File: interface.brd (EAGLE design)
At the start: 100 x 80 mm, 37 parts, among them U1 ATMEGA328P_PDIP

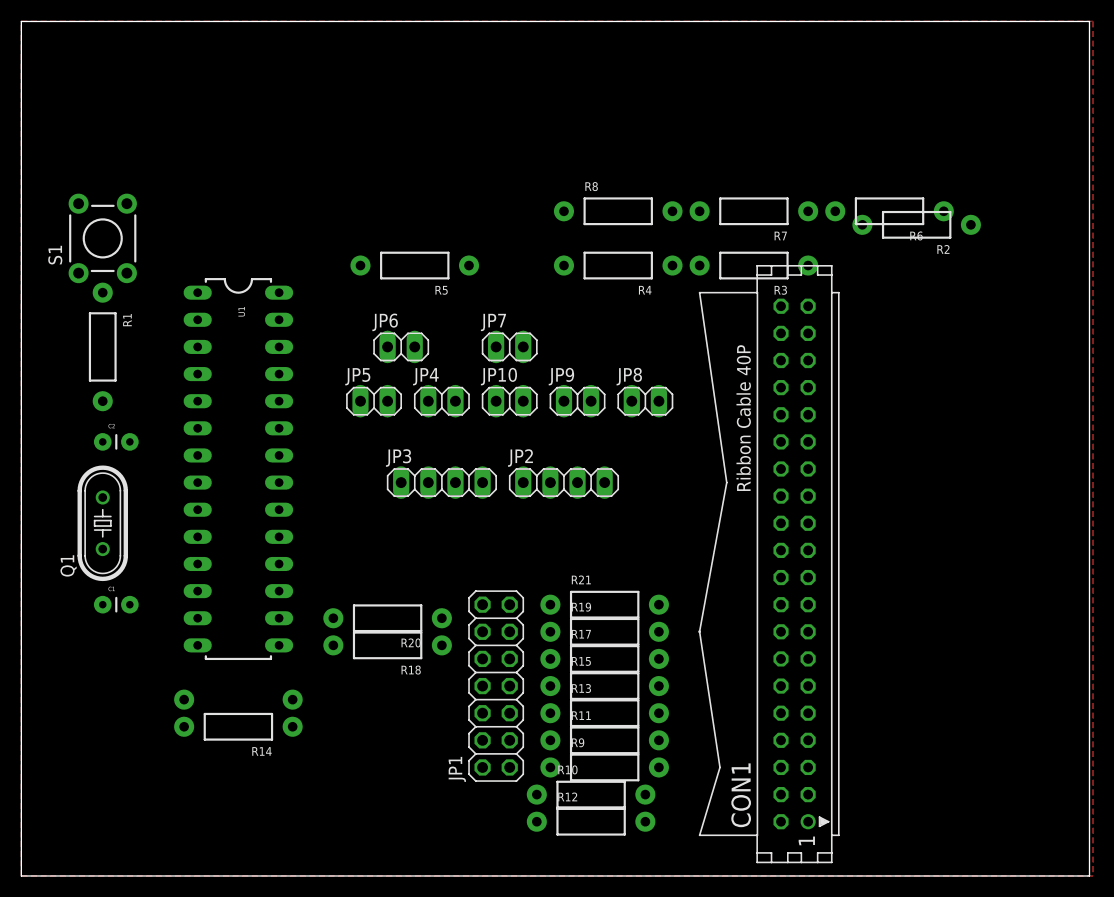
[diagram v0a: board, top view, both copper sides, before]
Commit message: Reorg the schematic. First pass at autorouter
Need to check if LED resistors will affect XBox circuitry
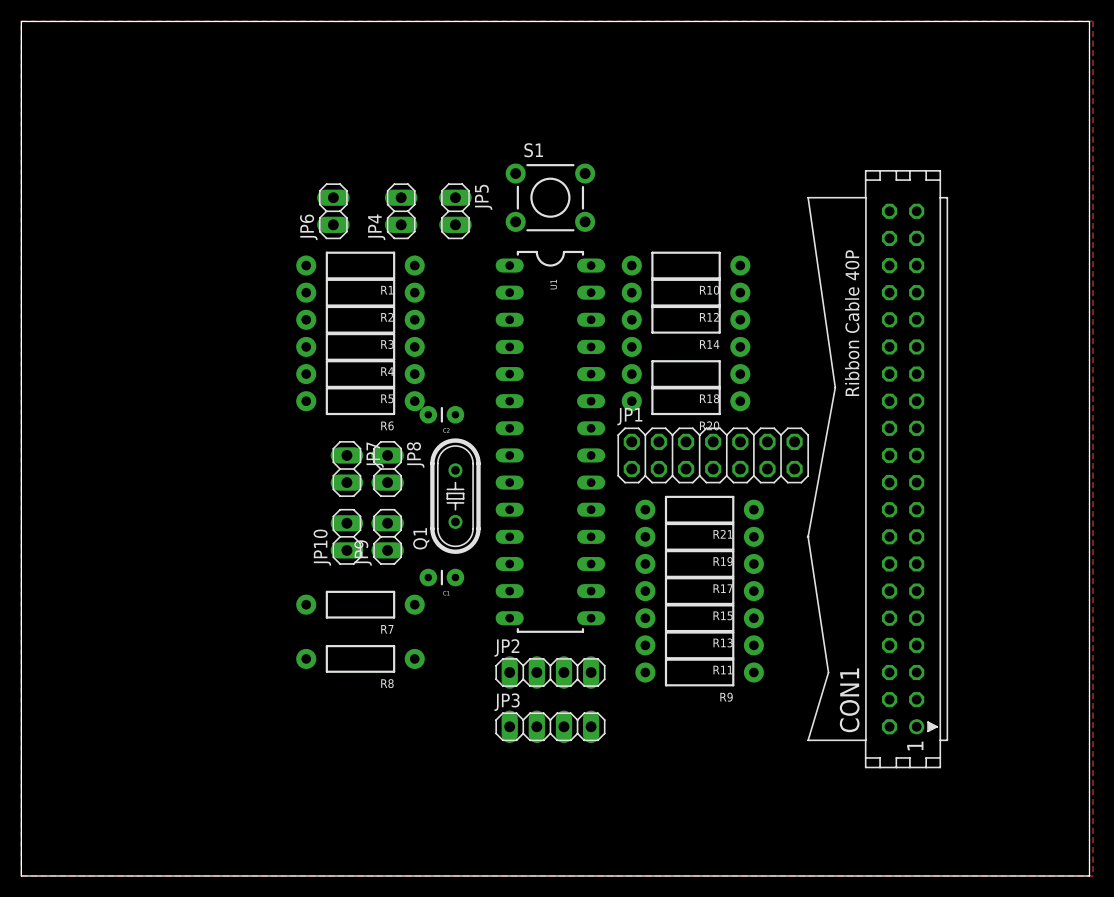
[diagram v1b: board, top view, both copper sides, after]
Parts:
- moved R14 56.6 mm to (62.2, 52.1)
- moved R16 53.4 mm to (62.2, 49.5)
- moved R6 52.6 mm to (31.8, 44.5)
- moved R2 52.5 mm to (31.8, 54.6)
- moved R7 52.1 mm to (31.8, 25.4)
- moved R10 50.3 mm to (62.2, 57.1), turned to 180 degrees
- moved R12 50.3 mm to (62.2, 54.6), turned to 180 degrees
- moved R8 48.4 mm to (31.8, 20.3), turned to 180 degrees
- moved S1 42.1 mm to (49.5, 63.5), turned to 0 degrees
- moved R18 37.8 mm to (62.2, 47.0)
- moved R3 37.2 mm to (31.8, 52.1)
- moved R20 34.5 mm to (62.2, 44.5)
- moved C1 33.1 mm to (40.6, 27.9), turned to 180 degrees
- moved C2 33.1 mm to (40.6, 43.2), turned to 180 degrees
- moved Q1 33.1 mm to (40.6, 35.6)
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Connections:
- net BTN1: now also U1.2
- net BTN2: now also U1.3; no longer U1.24
- net BTN3: now also U1.4; no longer U1.25
- net BTN4: now also U1.5; no longer U1.26
- net BTN5: now also U1.6; no longer U1.27
- net BTN6: now also U1.11; no longer U1.28
- net BTN7: now also U1.12; no longer U1.2
- net N$10: now also U1.16; no longer CON1.26, U1.13
- net N$11: now also CON1.22, JP1.7, R15.P$1; no longer CON1.24, R14.P$2, U1.12
- net N$12: now also CON1.24, JP1.9, R17.P$1; no longer CON1.22, R13.P$2, U1.11
- net N$13: now also R17.P$2, U1.17; no longer CON1.20, R12.P$2, U1.6
- net N$14: now also R19.P$2, U1.18; no longer CON1.18, R11.P$2, U1.5
- net N$15: now also R21.P$2, U1.19; no longer CON1.16, R10.P$2, U1.4
- net N$16: now also CON1.28, JP1.13, R21.P$1; no longer CON1.14, R9.P$2
- net N$21: now also CON1.26, JP1.11, R19.P$1; no longer JP1.1, R9.P$1
- net N$22: now also R10.P$2, U1.28; no longer JP1.2, R10.P$1
- net N$23: now also CON1.14, JP1.2, R10.P$1; no longer JP1.3, R11.P$1
- net N$24: now also R12.P$2, U1.27; no longer JP1.4, R12.P$1
- net N$25: now also CON1.12, JP1.4, R12.P$1; no longer JP1.5, R13.P$1
- net N$26: now also R14.P$2, U1.26; no longer JP1.6, R14.P$1
- net N$27: now also CON1.10, JP1.6, R14.P$1; no longer JP1.7, R15.P$1
- net N$28: now also R16.P$2, U1.25; no longer JP1.8, R16.P$1
- net N$29: now also CON1.8, JP1.8, R16.P$1; no longer JP1.9, R17.P$1
- net N$30: now also R18.P$2, U1.24; no longer JP1.10, R18.P$1
- net N$31: now also CON1.6, JP1.10, R18.P$1; no longer JP1.11, R19.P$1
- net N$32: now also R20.P$2, U1.23; no longer JP1.12, R20.P$1
- net N$33: now also CON1.4, JP1.12, R20.P$1; no longer JP1.13, R21.P$1
- net N$4: now also R9.P$2, U1.13; no longer CON1.28, R16.P$2, U1.14
- net N$5: now also CON1.16, JP1.1, R9.P$1; no longer CON1.30, R17.P$2, U1.15
- net N$6: now also R11.P$2, U1.14; no longer CON1.32, R18.P$2, U1.16
- net N$7: now also CON1.18, JP1.3, R11.P$1; no longer CON1.34, R19.P$2, U1.17
- net N$8: now also CON1.20, JP1.5, R13.P$1; no longer CON1.36, R20.P$2, U1.18
- net N$9: now also R13.P$2, U1.15; no longer CON1.38, R21.P$2, U1.19

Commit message: Resized, first pass completed
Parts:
- moved JP10 25.7 mm to (6.35, 22.9)
- moved JP2 25.7 mm to (25.4, 10.2)
- moved JP3 25.7 mm to (25.4, 5.08)
- moved JP7 25.7 mm to (6.35, 29.2)
- moved R11 25.7 mm to (39.4, 12.7)
- moved R13 25.7 mm to (39.4, 15.2)
- moved R15 25.7 mm to (39.4, 17.8)
- moved R17 25.7 mm to (39.4, 20.3)
- moved R19 25.7 mm to (39.4, 22.9)
- moved R21 25.7 mm to (39.4, 25.4)
- moved R9 25.7 mm to (39.4, 10.2)
- moved S1 25.7 mm to (25.4, 54.6)
- moved U1 25.7 mm to (25.4, 31.8)
- moved JP8 25.7 mm to (10.2, 29.2)
- moved JP9 25.7 mm to (10.2, 22.9)
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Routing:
- net VCC: track 0.00 -> 131.5 mm
- net N$23: track 0.00 -> 54.4 mm
- net N$25: track 0.00 -> 50.9 mm
- net N$27: track 0.00 -> 47.3 mm
- net N$18: track 0.00 -> 46.9 mm
- net N$17: track 0.00 -> 46.9 mm
- net N$29: track 0.00 -> 43.7 mm
- net N$5: track 0.00 -> 41.7 mm
- net N$31: track 0.00 -> 41.5 mm
- net N$7: track 0.00 -> 38.2 mm
- net N$20: track 0.00 -> 37.7 mm
- net N$19: track 0.00 -> 34.6 mm
- net N$8: track 0.00 -> 34.6 mm
- net N$33: track 0.00 -> 33.7 mm
- net N$11: track 0.00 -> 31.0 mm
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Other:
- board size 100 x 80 mm -> 64.4 x 61 mm
